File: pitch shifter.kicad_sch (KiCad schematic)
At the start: 3 parts, among them U2 STM32G030K8T6, U3 PCM3060PWR

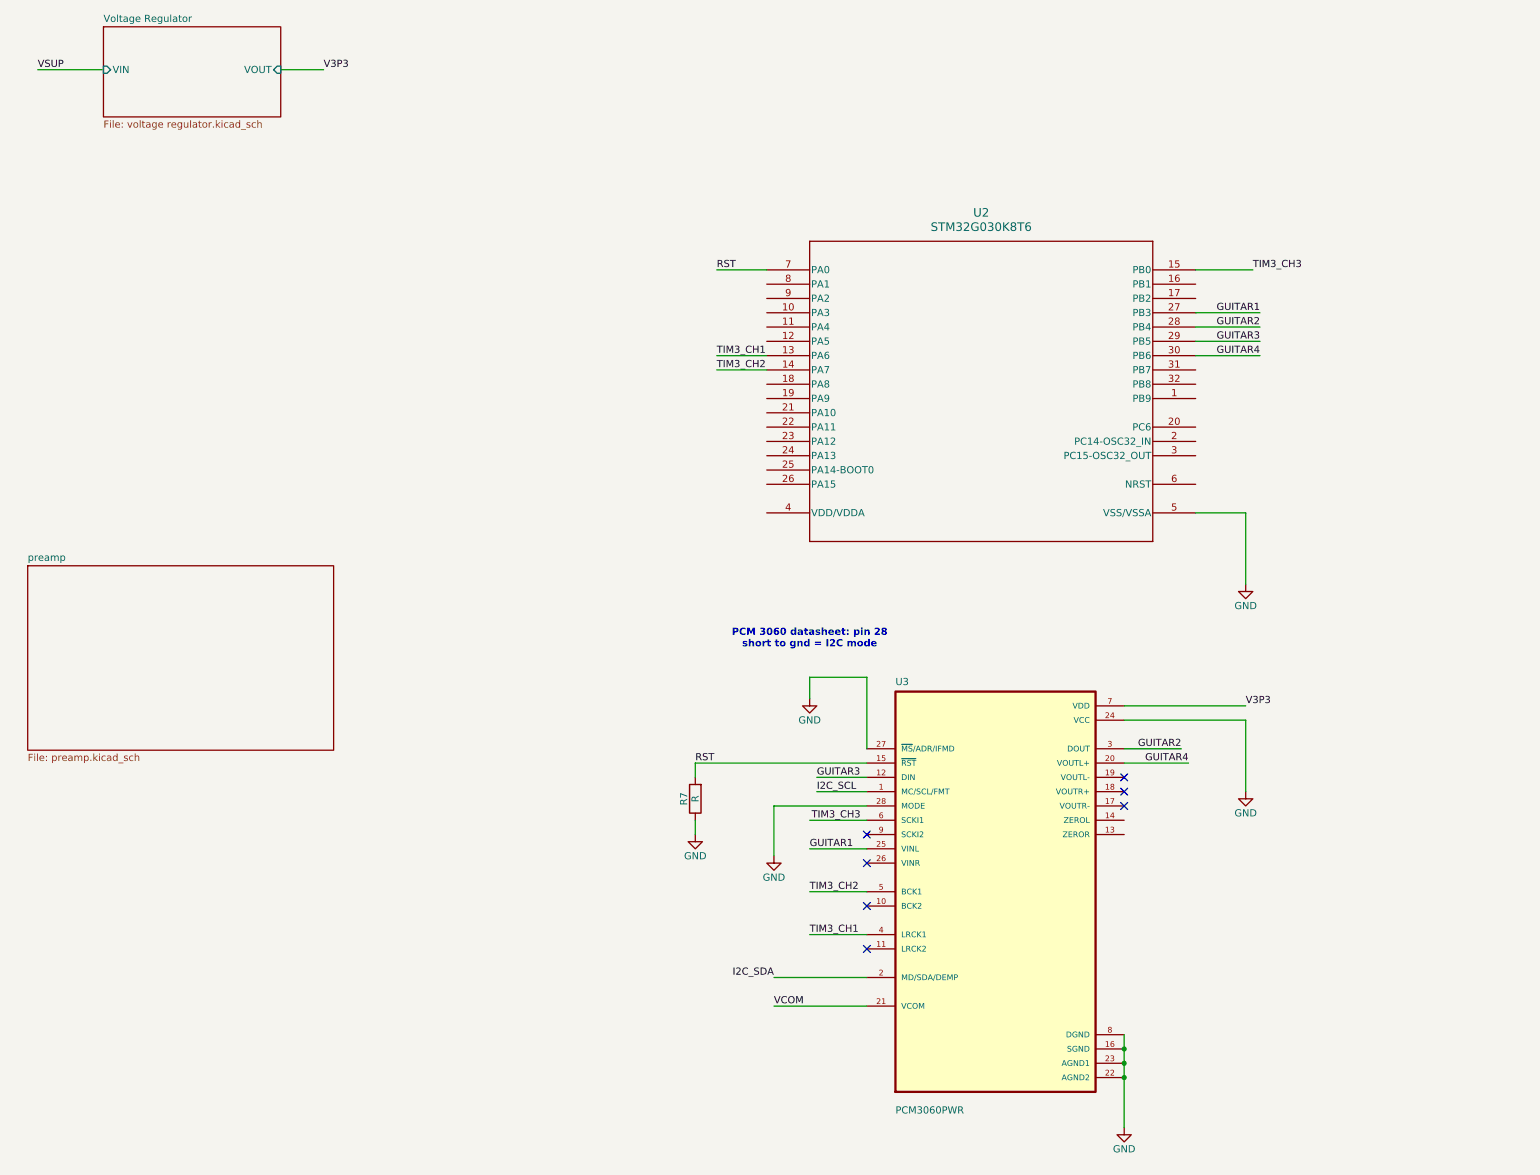
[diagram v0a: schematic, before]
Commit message: added power and output switches
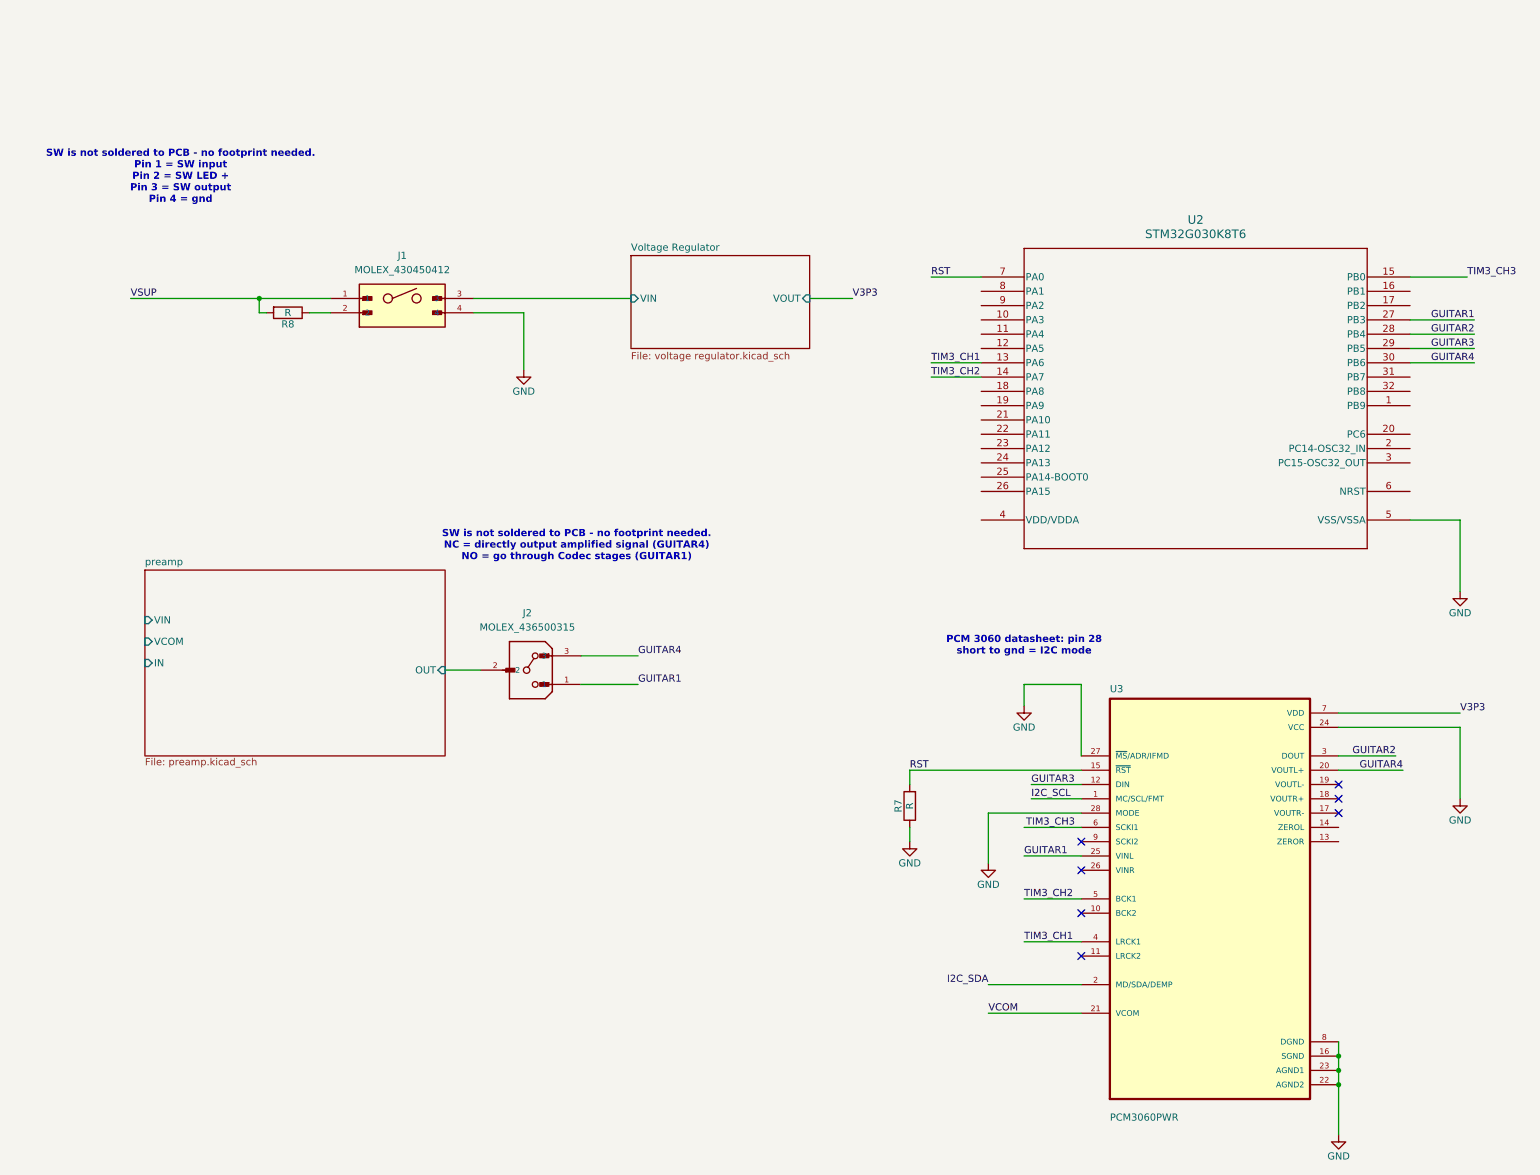
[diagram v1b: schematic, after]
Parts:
- added J1: MOLEX_430450412, Project_Components:MOLEX_430450412, symbol Project_Components:MOLEX_430450412
- added J2: MOLEX_436500315, Project_Components:MOLEX_436500315, symbol Project_Components:MOLEX_436500315
- added R8: R, symbol Device:R
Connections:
- net GND: now also J1.4
- net GUITAR1: now also J2.1
- net GUITAR4: now also J2.3
- net VSUP: now also J1.1, R8.2
- net Voltage Regulator/VIN: now also J1.3
- new net: J1.2, R8.1
- new net preamp/OUT: J2.2
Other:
- sheet preamp ports: added IN, OUT, VCOM, VIN; removed none
- note added: "SW is not soldered to PCB - no footprint needed. NC = directly output amplified signal (GUITAR4) NO = go through Codec stages (GUITAR1)"
- note added: "SW is not soldered to PCB - no footprint needed. Pin 1 = SW input Pin 2 = SW LED + Pin 3 = SW output Pin 4 = gnd"
- moved on the sheet: R7, U2, U3

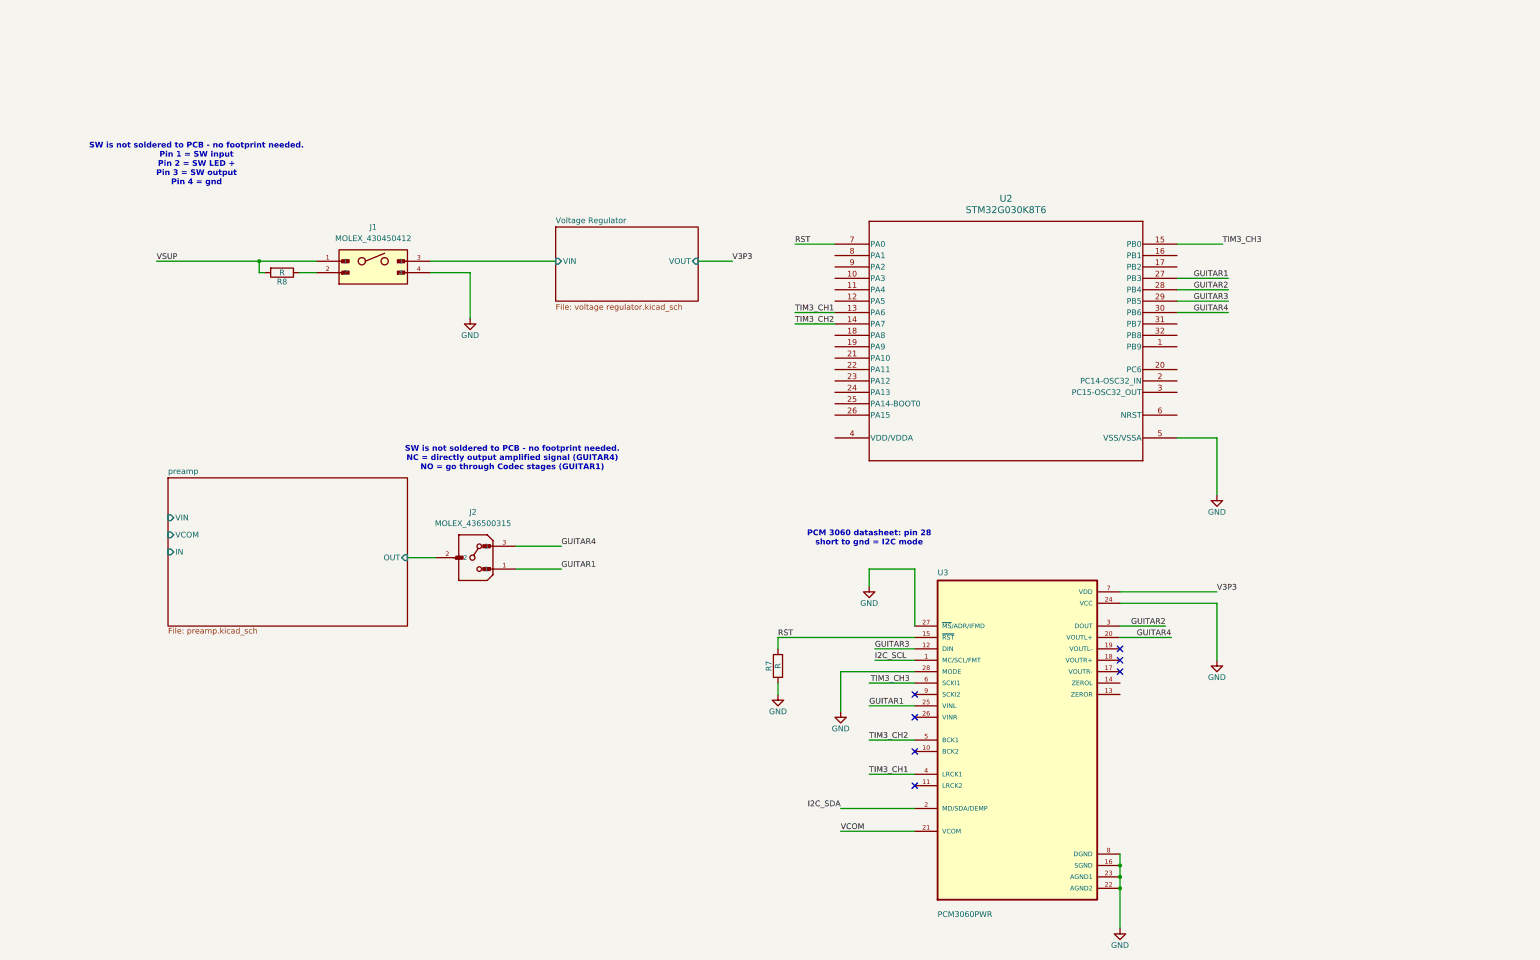
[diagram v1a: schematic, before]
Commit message: Add oscillator, mounting holes, switches
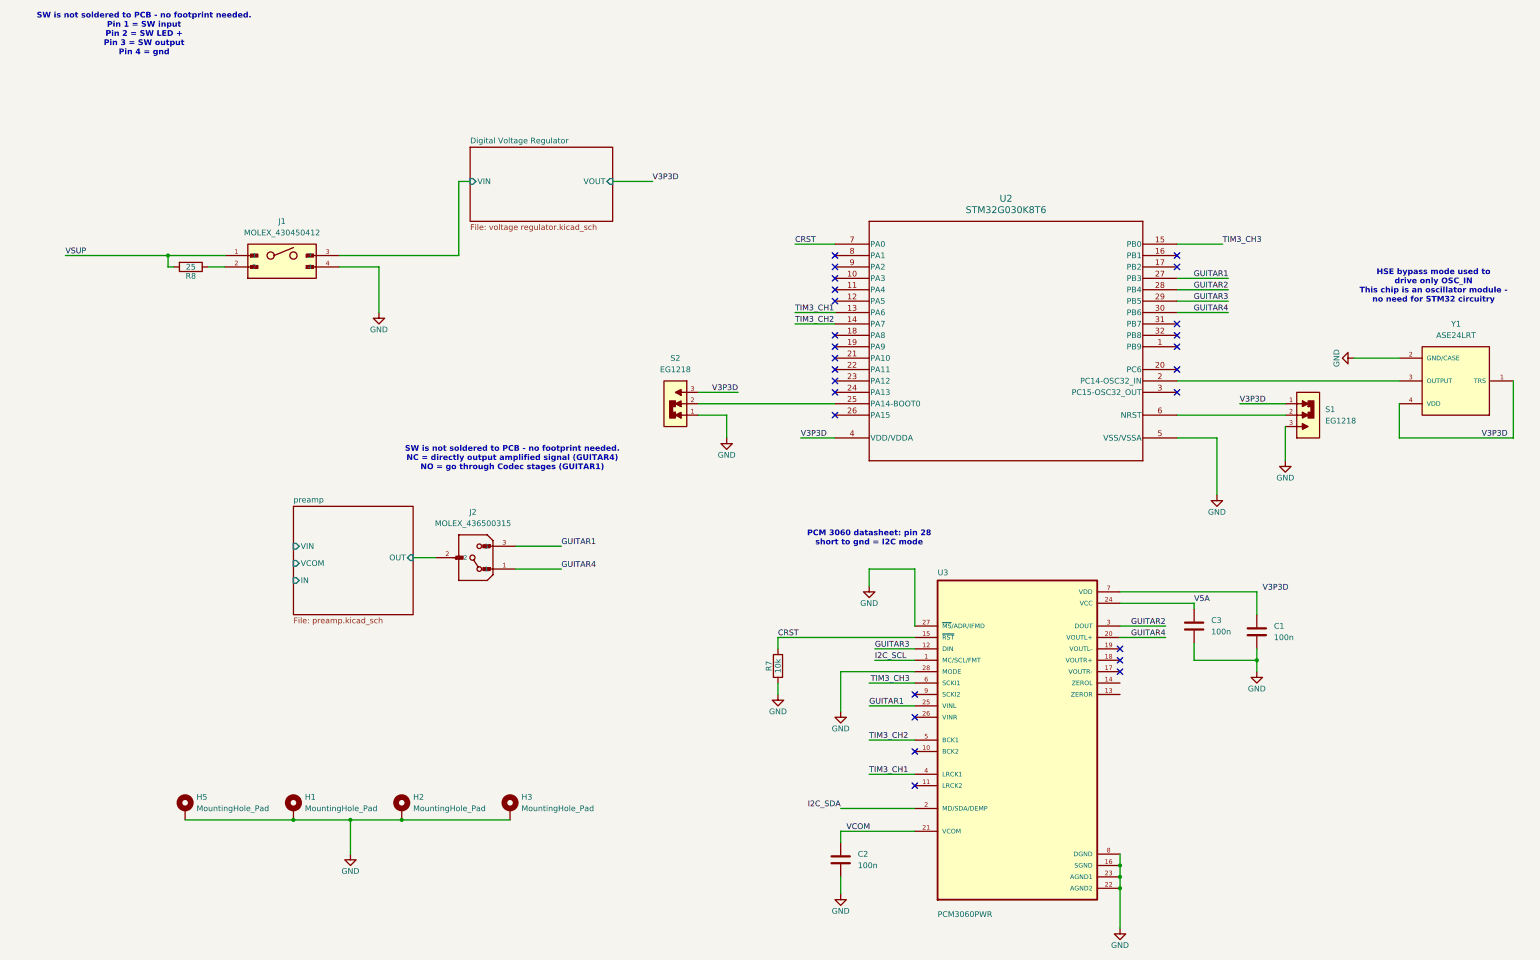
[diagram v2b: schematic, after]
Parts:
- added C1, C2, C3: 100n, Capacitor_SMD:C_0201_0603Metric_Pad0.64x0.40mm_HandSolder, symbol Device:C
- added H1, H2, H3, H5: MountingHole_Pad, MountingHole:MountingHole_3.2mm_M3_Pad_Via, symbol Mechanical:MountingHole_Pad
- added S1, S2: EG1218, Project_Components:EG1218, symbol Project_Components:EG1218
- added Y1: ASE24LRT, Project_Components:ASE24LRT, symbol Project_Components:ASE24LRT
- R7: value R -> 10k; footprint (none) -> Resistor_SMD:R_0603_1608Metric_Pad0.98x0.95mm_HandSolder
- R8: value R -> 25; footprint (none) -> Resistor_SMD:R_0603_1608Metric_Pad0.98x0.95mm_HandSolder
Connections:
- net GND: now also C1.2, C2.2, C3.2, H1.1, H2.1, H3.1, H5.1, S1.3, S2.1, Y1.2 (GND/CASE); no longer U3.24 (VCC)
- net GUITAR1: now also J2.3; no longer J2.1
- net GUITAR4: now also J2.1; no longer J2.3
- net VCOM: now also C2.1
- net at U2.2 (PC14-OSC32_IN): now also Y1.3 (OUTPUT)
- net at U2.25 (PA14-BOOT0): now also S2.2
- net V3P3D: now reaches U2.4 (VDD/VDDA)
- net V3P3D: now also S1.1, S2.3, Y1.1 (TRS), Y1.4 (VDD)
- net at U2.6 (NRST): now also S1.2
- net RST renamed CRST
- net V3P3: no longer names the net of U3.7 (VDD)
- net V3P3: now also C1.1
- net Voltage Regulator/VIN renamed Digital Voltage Regulator/VIN
- new net V5A: C3.1, U3.24 (VCC)
- no-connect marks 7 -> 26
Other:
- removed sheet Voltage Regulator
- added sheet Digital Voltage Regulator (voltage regulator.kicad_sch)
- note added: "HSE bypass mode used to drive only OSC_IN This chip is an oscillator module - no need for STM32 circuitry"
- moved on the sheet: J1, R8
